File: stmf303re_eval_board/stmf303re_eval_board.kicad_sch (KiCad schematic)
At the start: 31 parts, among them J1 Conn_01x04_Male, J2 USB_B_Micro, J3 Conn_01x16, J4 Conn_01x16, SW1 SW_DPST_x2, U1 STM32F303RETx, U2 XC6206PxxxMR, Y1 8MHz

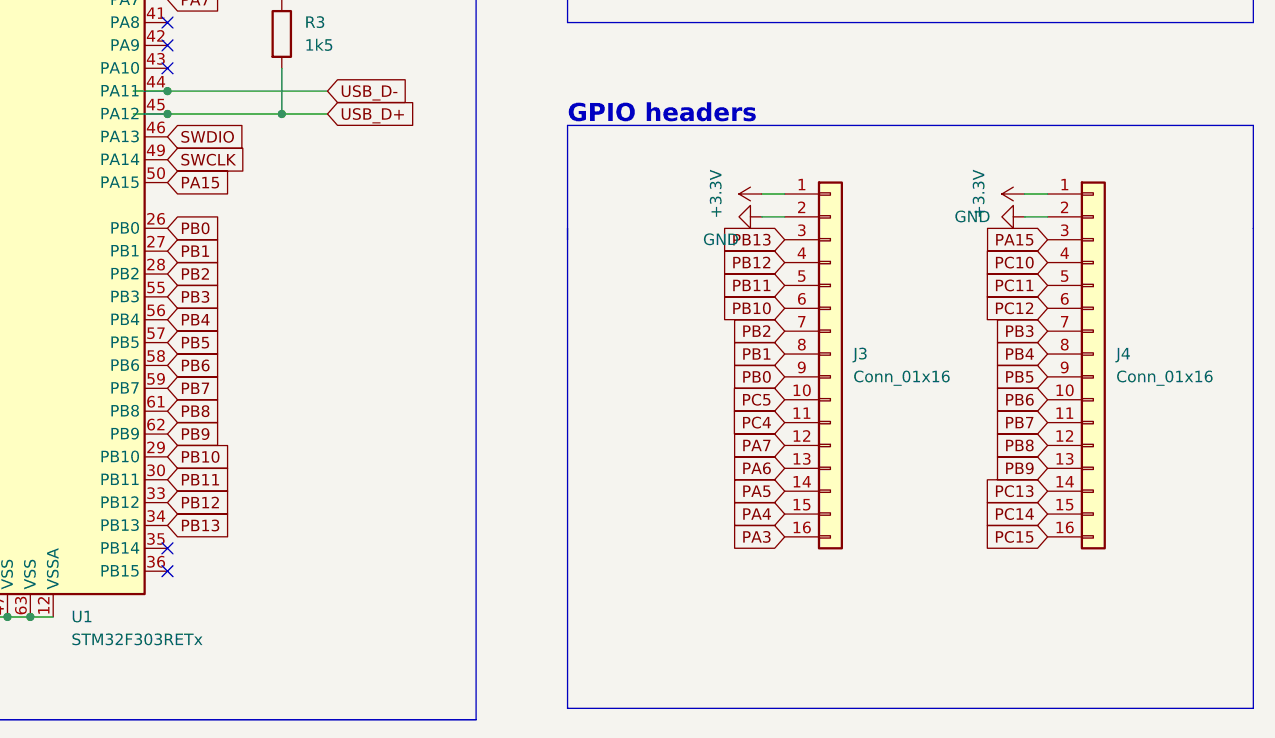
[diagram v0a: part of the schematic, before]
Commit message: usb, traces fixed
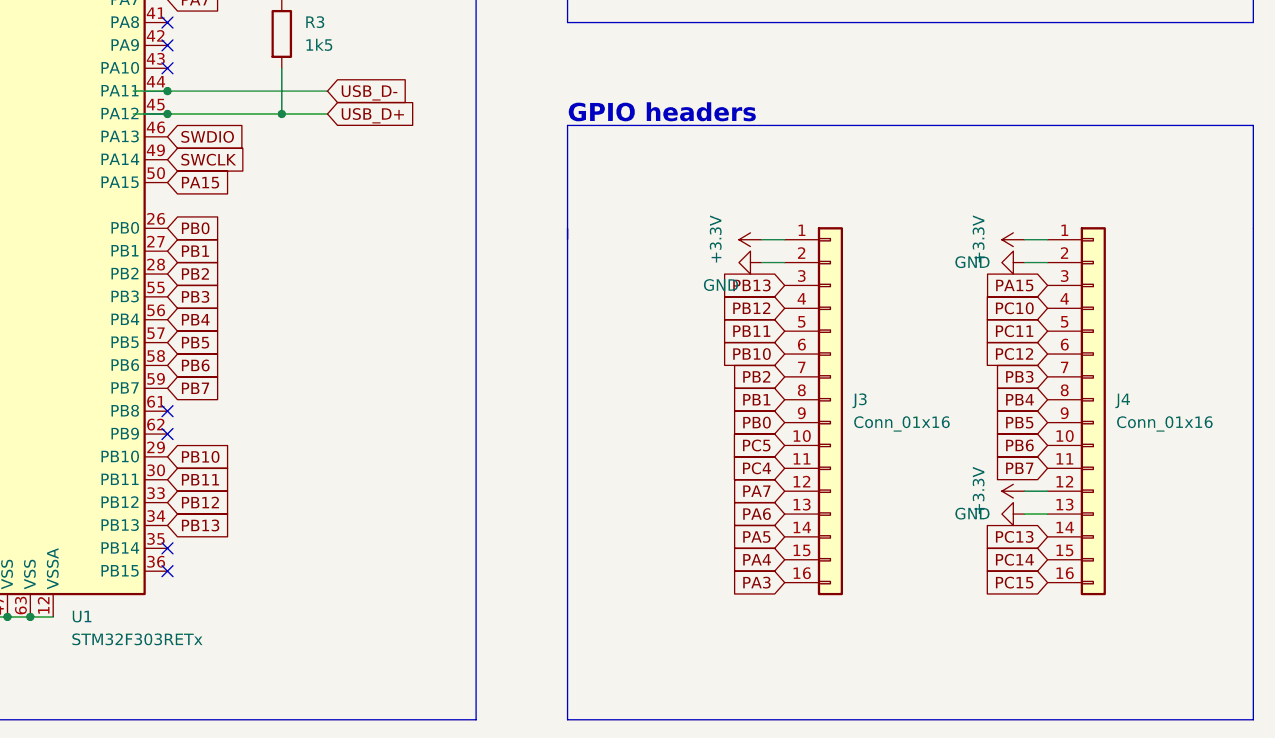
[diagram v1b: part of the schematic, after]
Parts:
- J2: footprint Connector_USB:USB_Micro-B_Wuerth_629105150521 -> Connector_USB:USB_Micro-B_Molex_47346-0001
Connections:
- net +3.3V: now also J4.12 (Pin_12)
- net GND: now also J4.13 (Pin_13)
- net PB8: no longer names the net of U1.61 (PB8)
- net PB8: no longer J4.12 (Pin_12)
- net PB9: no longer names the net of U1.62 (PB9)
- net PB9: no longer J4.13 (Pin_13)
- no-connect marks 18 -> 20
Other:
- moved on the sheet: J3, J4

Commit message: traces update
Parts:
- J3, J4: footprint Connector_PinHeader_2.54mm:PinHeader_1x16_P2.54mm_Vertical -> Connector_PinSocket_2.54mm:PinSocket_1x16_P2.54mm_Vertical
- Y1: footprint Crystal:Crystal_SMD_5032-2Pin_5.0x3.2mm -> Crystal:Crystal_SMD_0603-2Pin_6.0x3.5mm
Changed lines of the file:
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@@
       (effects (font (size 1.27 1.27)) (justify left))
     )
-    (property "Footprint" "Connector_PinHeader_2.54mm:PinHeader_1x16_P2.54mm_Vertical" (id 2) (at 226.06 101.6 0)
+    (property "Footprint" "Connector_PinSocket_2.54mm:PinSocket_1x16_P2.54mm_Vertical" (id 2) (at 226.06 101.6 0)
       (effects (font (size 1.27 1.27)) hide)
     )
@@
       (effects (font (size 1.27 1.27)) (justify left))
     )
-    (property "Footprint" "Connector_PinHeader_2.54mm:PinHeader_1x16_P2.54mm_Vertical" (id 2) (at 255.27 101.6 0)
+    (property "Footprint" "Connector_PinSocket_2.54mm:PinSocket_1x16_P2.54mm_Vertical" (id 2) (at 255.27 101.6 0)
       (effects (font (size 1.27 1.27)) hide)
     )
@@
     (property "Reference" "Y1" (id 0) (at 95.25 67.31 0))
     (property "Value" "8MHz" (id 1) (at 95.25 69.85 0))
-    (property "Footprint" "Crystal:Crystal_SMD_5032-2Pin_5.0x3.2mm" (id 2) (at 95.25 74.93 0)
+    (property "Footprint" "Crystal:Crystal_SMD_0603-2Pin_6.0x3.5mm" (id 2) (at 95.25 74.93 0)
       (effects (font (size 1.27 1.27)) hide)
     )
@@
     )
     (path "/23571b3a-a5ca-4c10-9862-a138d65d8fd4"
-      (reference "J3") (unit 1) (value "Conn_01x16") (footprint "Connector_PinHeader_2.54mm:PinHeader_1x16_P2.54mm_Vertical")
+      (reference "J3") (unit 1) (value "Conn_01x16") (footprint "Connector_PinSocket_2.54mm:PinSocket_1x16_P2.54mm_Vertical")
     )
     (path "/4895e6a5-db02-467a-9afe-63950993cf82"
-      (reference "J4") (unit 1) (value "Conn_01x16") (footprint "Connector_PinHeader_2.54mm:PinHeader_1x16_P2.54mm_Vertical")
+      (reference "J4") (unit 1) (value "Conn_01x16") (footprint "Connector_PinSocket_2.54mm:PinSocket_1x16_P2.54mm_Vertical")
     )
     (path "/0dec8f18-1dfd-4160-a214-6c2d501d7b9e"
@@
     )
     (path "/80968213-3579-4765-ad24-9da0eb9f99fa"
-      (reference "Y1") (unit 1) (value "8MHz") (footprint "Crystal:Crystal_SMD_5032-2Pin_5.0x3.2mm")
-    )
-  )
+      (reference "Y1") (unit 1) (value "8MHz") (footprint "Crystal:Crystal_SMD_0603-2Pin_6.0x3.5mm")
+    )
+  )
